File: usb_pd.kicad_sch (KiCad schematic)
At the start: 39 parts, among them J1 USB-C_GCT_USB4105-GF-A, J2 JST_SH_1x4_SM04B-SRSS-TB-LF-SN, Q1 SQS401EN-T1_BE3, U1 STUSB4500_QFN, U5 TPD4E02B04DQA, U6 TPD4E02B04DQA

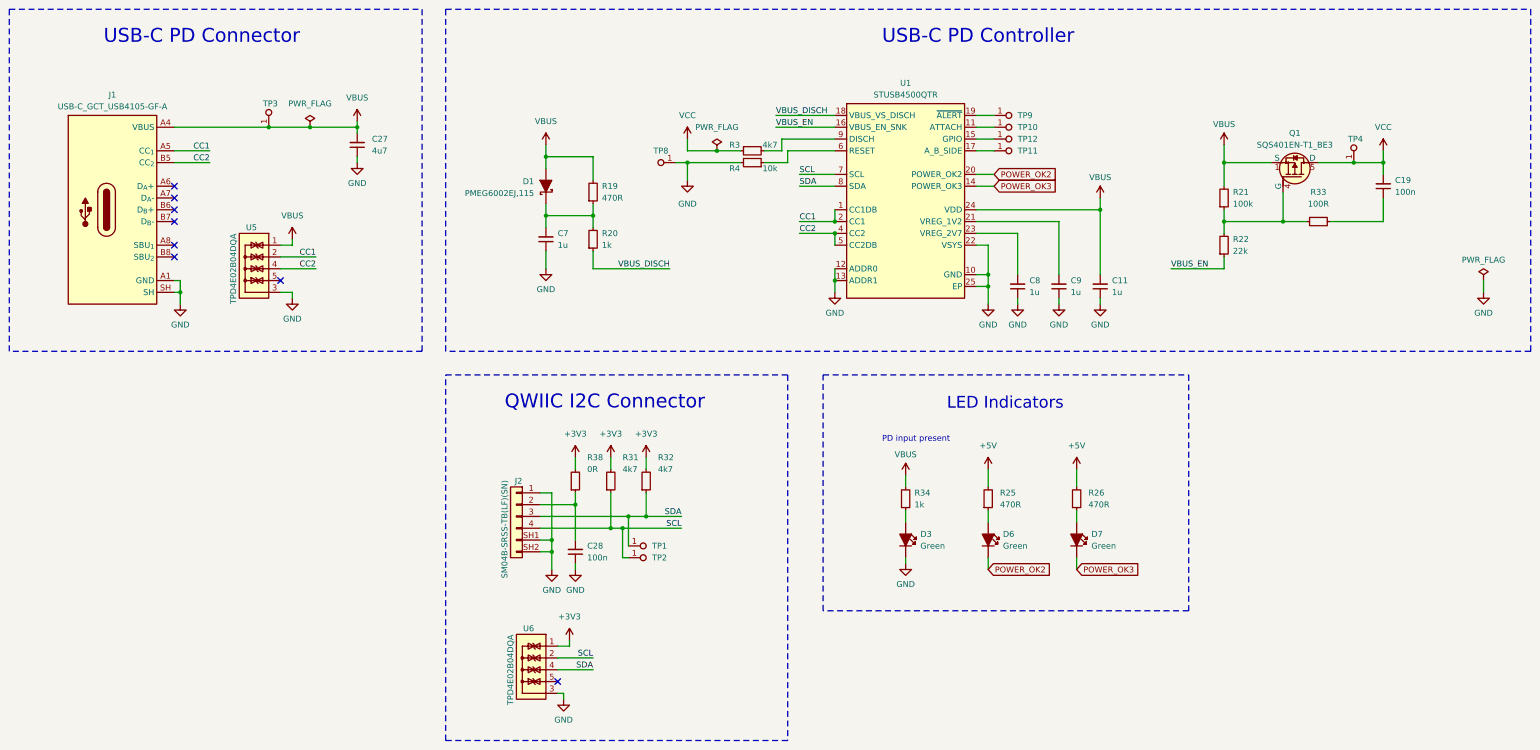
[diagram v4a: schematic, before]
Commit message: [#57006] Add tranzistor on D3
PD input present LED
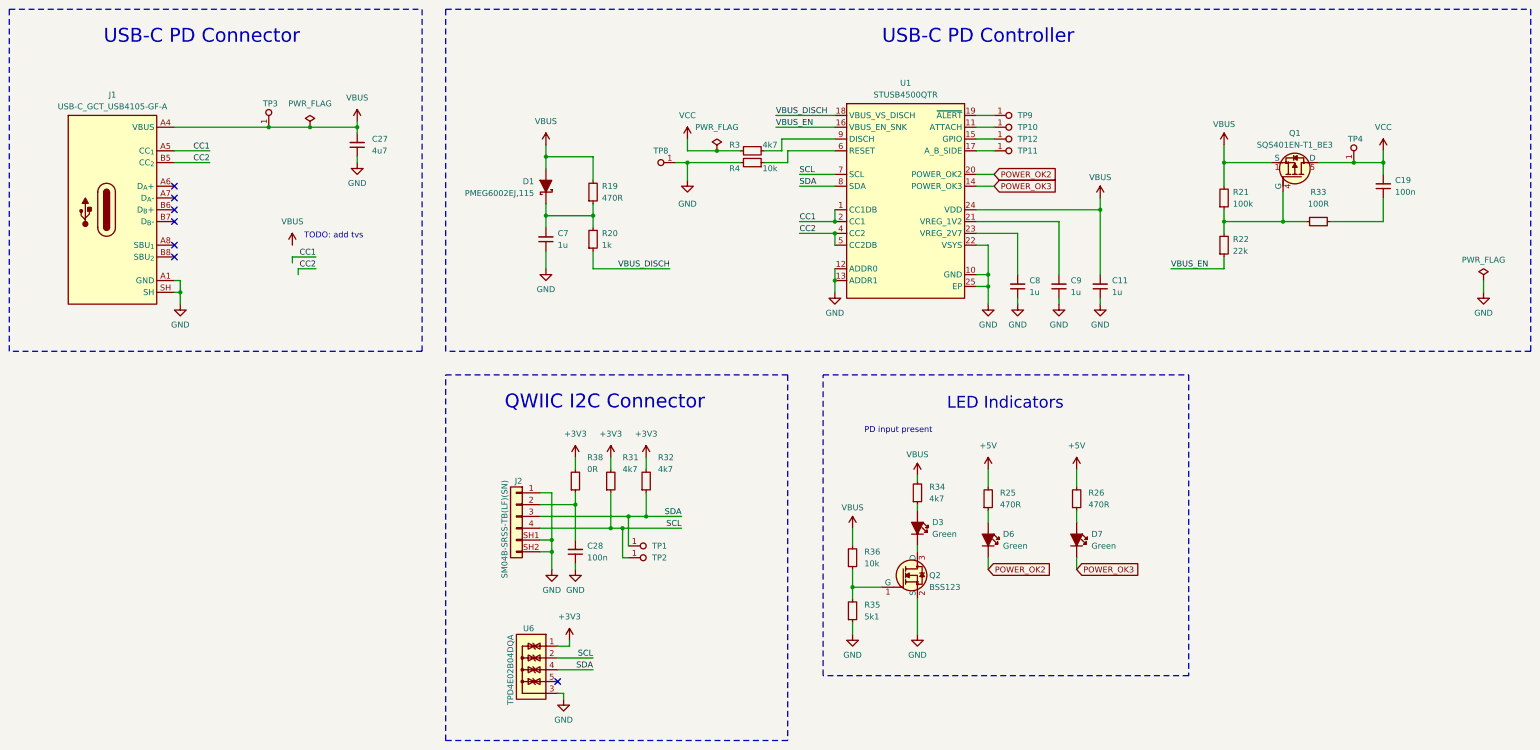
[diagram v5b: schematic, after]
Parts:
- removed R34: R_2k2_0402, antmicro-footprints:R_0402_1005Metric, symbol antmicroResistors0402:R_1k_0402
- removed U5: TPD4E02B04DQA, antmicro-footprints:USON-10_2.5x1mm_P0.5mm, symbol antmicroTVSDiodes:TPD4E02B04DQA
- added Q2: BSS123, antmicro-footprints:SOT-23-3, symbol antmicroTransistorsFETsMOSFETsSingle:BSS123
- added R34: R_4k7_0402, antmicro-footprints:R_0402_1005Metric, symbol antmicroResistors0402:R_4k7_0402
- added R35: R_5k1_0402, antmicro-footprints:R_0402_1005Metric, symbol antmicroResistors0402:R_5k1_0402
- added R36: R_10k_0402, antmicro-footprints:R_0402_1005Metric, symbol antmicroResistors0402:R_10k_0402
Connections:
- net GND: now also Q2.2 (S), R35.1; no longer D3.2
- net VBUS: now also R34.2, R36.2
- net at D3.1: now also R34.1
- new net: Q2.1 (G), R35.2, R36.1
- new net: D3.2, Q2.3 (D)
- no-connect marks 8 -> 7
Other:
- note added: "TODO: add tvs"
- moved on the sheet: D3

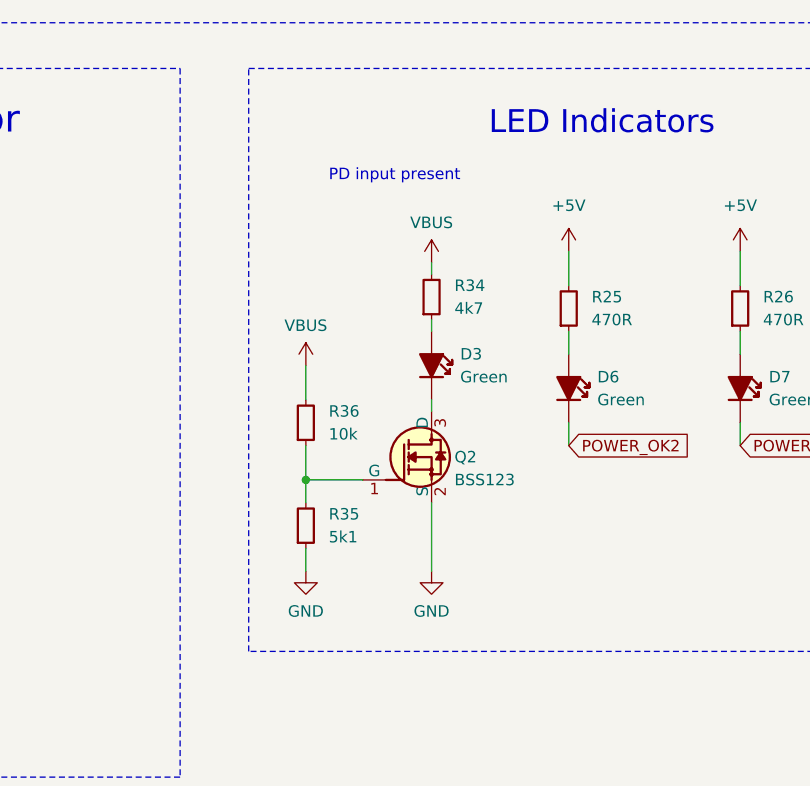
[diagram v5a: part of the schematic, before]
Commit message: [#57006] Remove tranzistor on D3
Change LED resistor's value
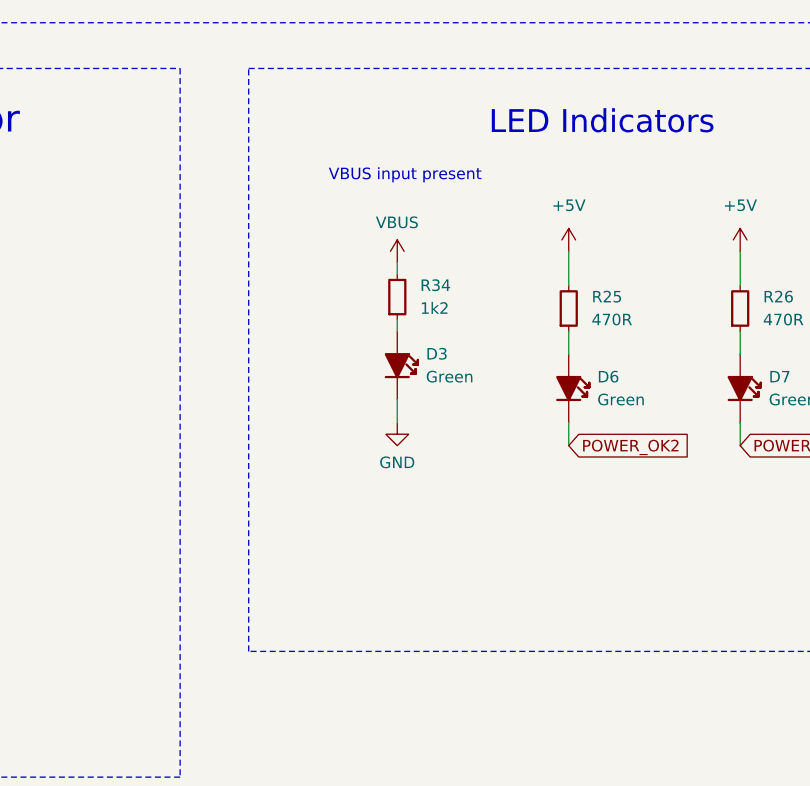
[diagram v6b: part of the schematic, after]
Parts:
- removed Q2: BSS123, antmicro-footprints:SOT-23-3, symbol antmicroTransistorsFETsMOSFETsSingle:BSS123
- removed R34: R_4k7_0402, antmicro-footprints:R_0402_1005Metric, symbol antmicroResistors0402:R_4k7_0402
- removed R35: R_5k1_0402, antmicro-footprints:R_0402_1005Metric, symbol antmicroResistors0402:R_5k1_0402
- removed R36: R_10k_0402, antmicro-footprints:R_0402_1005Metric, symbol antmicroResistors0402:R_10k_0402
- added R34: R_1k2_0402, antmicro-footprints:R_0402_1005Metric, symbol antmicroResistors0402:R_1k2_0402
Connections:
- net GND: now also D3.2
- net VBUS: now also R34.2
- net at D3.1: now also R34.1
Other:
- note added: "VBUS input present"
- note removed: "PD input present"
- moved on the sheet: D3

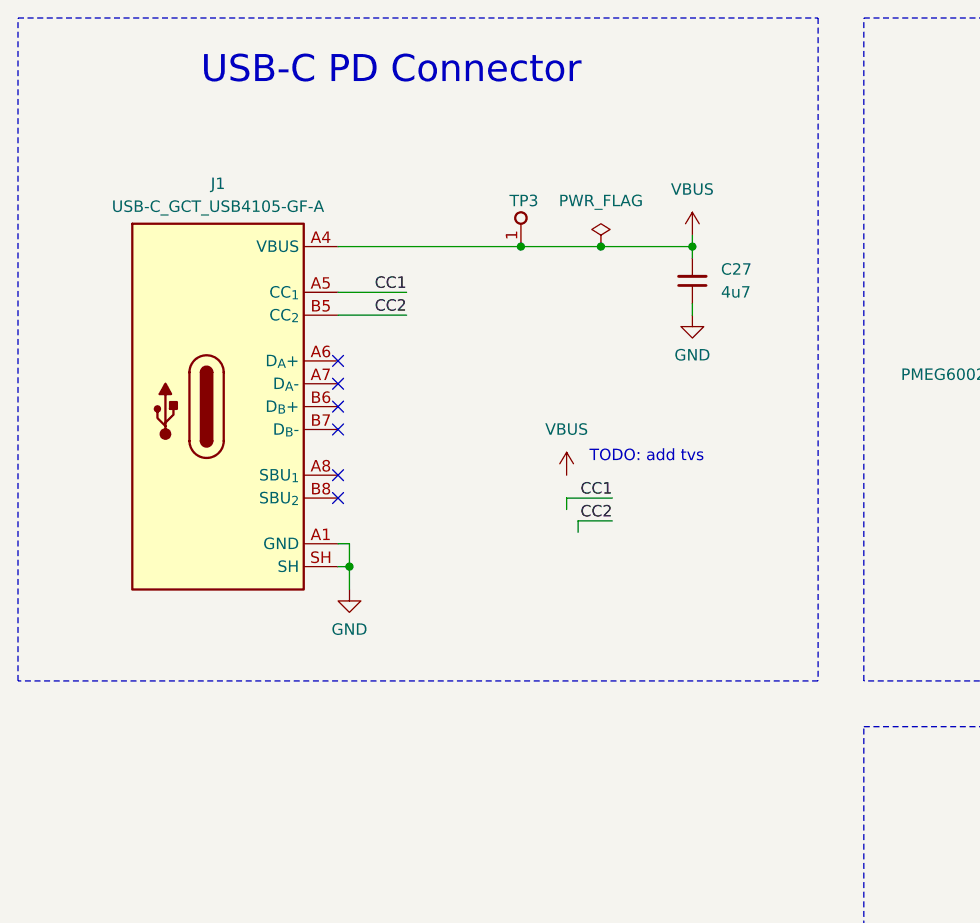
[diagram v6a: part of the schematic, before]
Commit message: [#57006] Add TVS2200DRVR on PD input
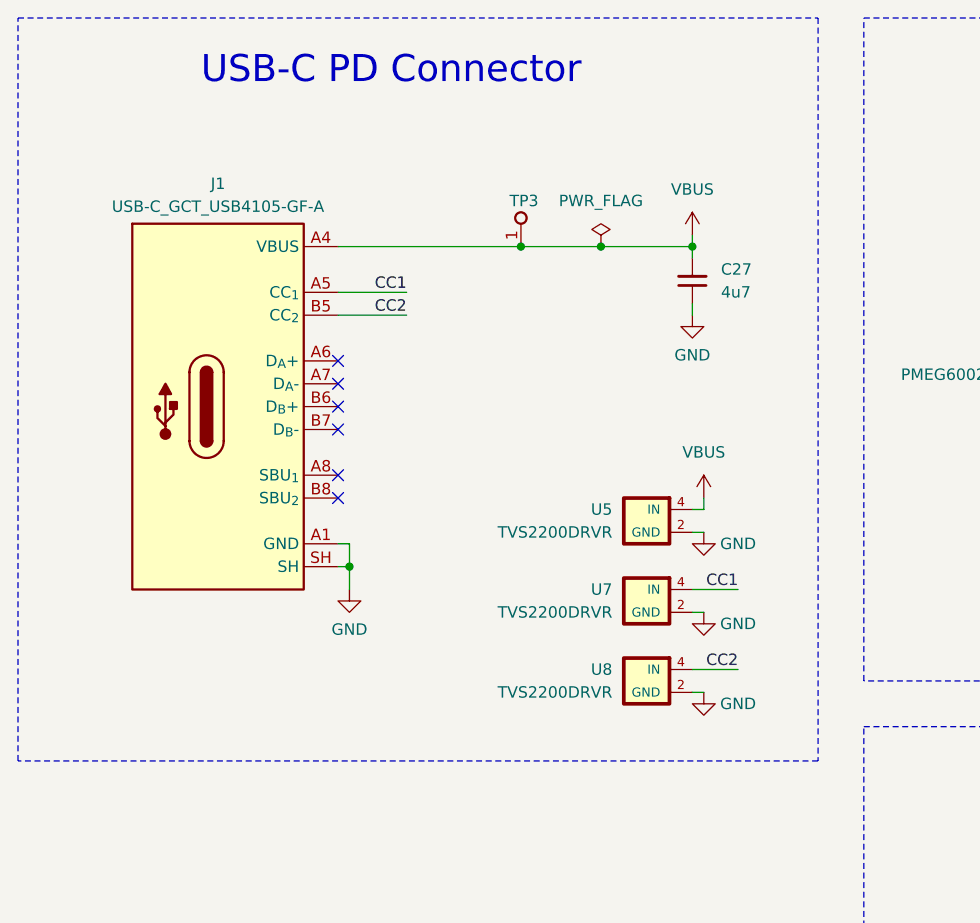
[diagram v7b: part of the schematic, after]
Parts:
- added U5, U7, U8: TVS2200DRVR, antmicro-footprints:WSON-6-1EP_2x2mm_P0.65mm, symbol antmicroTVSDiodes:TVS2200DRVR
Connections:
- net CC1: now also U7.4 (IN), U7.5 (IN), U7.6 (IN)
- net CC2: now also U8.4 (IN), U8.5 (IN), U8.6 (IN)
- net GND: now also U5.1 (GND), U5.2 (GND), U5.3 (GND), U5.7 (GND), U7.1 (GND), U7.2 (GND), U7.3 (GND), U7.7 (GND), U8.1 (GND), U8.2 (GND), U8.3 (GND), U8.7 (GND)
- net VBUS: now also U5.4 (IN), U5.5 (IN), U5.6 (IN)
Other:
- note removed: "TODO: add tvs"
